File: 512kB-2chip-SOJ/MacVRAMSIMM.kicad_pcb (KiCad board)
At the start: 4 copper layers, 102.9 x 20.3 mm, 17 parts, among them J1 VRAM, U1 42C8255, U2 42C8255

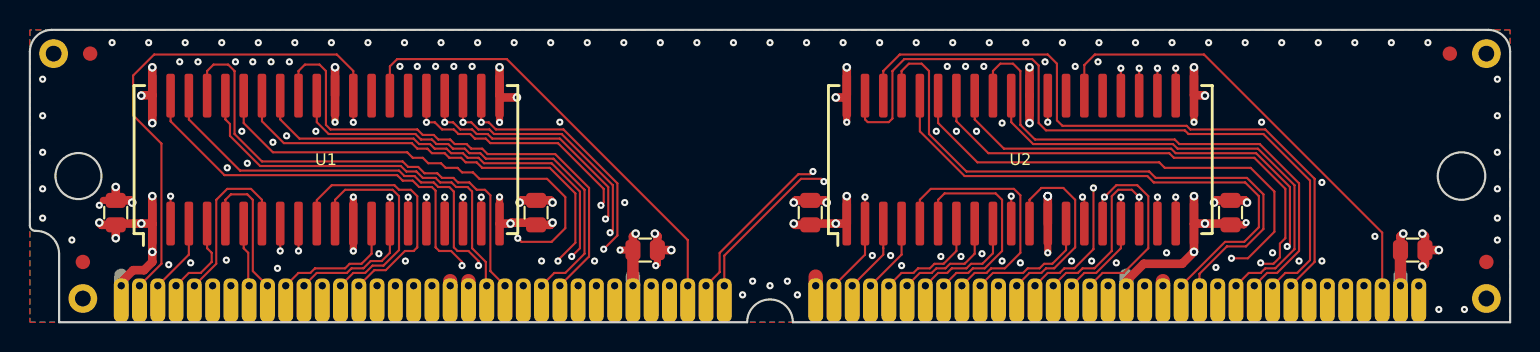
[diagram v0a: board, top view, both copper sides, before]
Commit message: Migrate to KiCAD 6
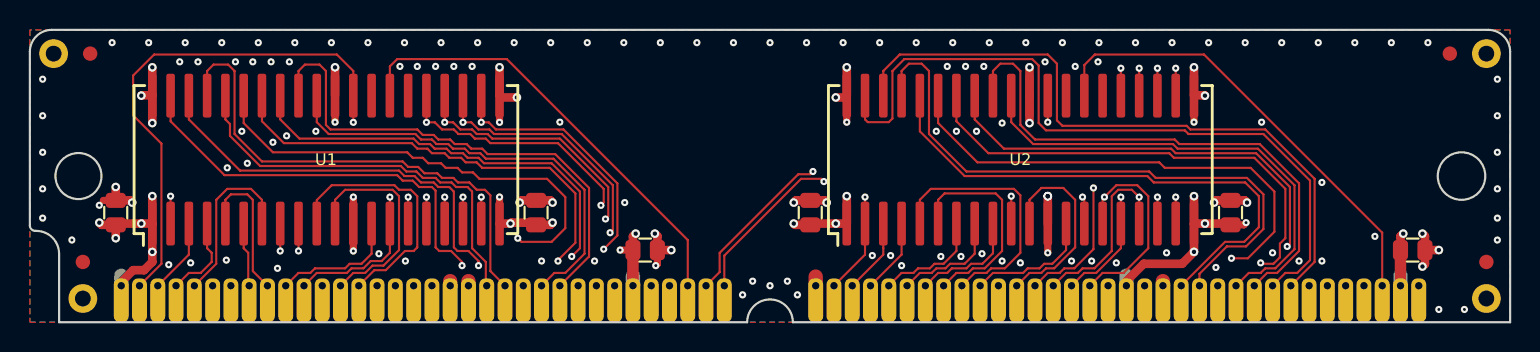
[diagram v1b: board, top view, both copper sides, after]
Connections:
- net /L~CAS~ renamed /L~{CAS}
- net /L~OE~ renamed /L~{OE}
- net /L~OE~2 renamed /L~{OE}2
- net /L~SE~ renamed /L~{SE}
- net /L~WE~ renamed /L~{WE}
- net /L~WE~2 renamed /L~{WE}2
- net /U~CAS~ renamed /U~{CAS}
- net /U~OE~ renamed /U~{OE}
- net /U~OE~2 renamed /U~{OE}2
- net /U~SE~ renamed /U~{SE}
- net /U~WE~ renamed /U~{WE}
- net /U~WE~2 renamed /U~{WE}2
- net /~RAS~ renamed /~{RAS}
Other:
- net class Default removed
